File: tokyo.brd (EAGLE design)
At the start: 115 x 34 mm, 49 parts, among them J1 254-2X5F, J2 254-2X5M, P1 9774050151, P2 9774050151, P3 9774050151, P4 9774050151, Q1 STD6N95K5, T1 750313823, U1 UCC28710, X1 508-1X3B

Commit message: Changed values of R13 and R14 in order to get +5.5V on output.
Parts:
- R13: value 24k9 -> 22k6
- R14: value 121k -> 118k
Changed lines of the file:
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@@
 <attribute name="NAME" x="71.185" y="25.3856" size="1.016" layer="26" ratio="10" rot="SMR90"/>
 </element>
-<element name="R14" library="resistors" package="0603" value="121k" x="55.02" y="7.07" smashed="yes" rot="MR0">
+<element name="R14" library="resistors" package="0603" value="118k" x="55.02" y="7.07" smashed="yes" rot="MR0">
 <attribute name="NAME" x="56.5444" y="5.075" size="1.016" layer="26" ratio="10" rot="SMR0"/>
 </element>
-<element name="R13" library="resistors" package="0603" value="24k9" x="51.93" y="7.43" smashed="yes" rot="MR270">
+<element name="R13" library="resistors" package="0603" value="22k6" x="51.93" y="7.43" smashed="yes" rot="MR270">
 <attribute name="NAME" x="51.475" y="3.6456" size="1.016" layer="26" ratio="10" rot="SMR90"/>
 </element>

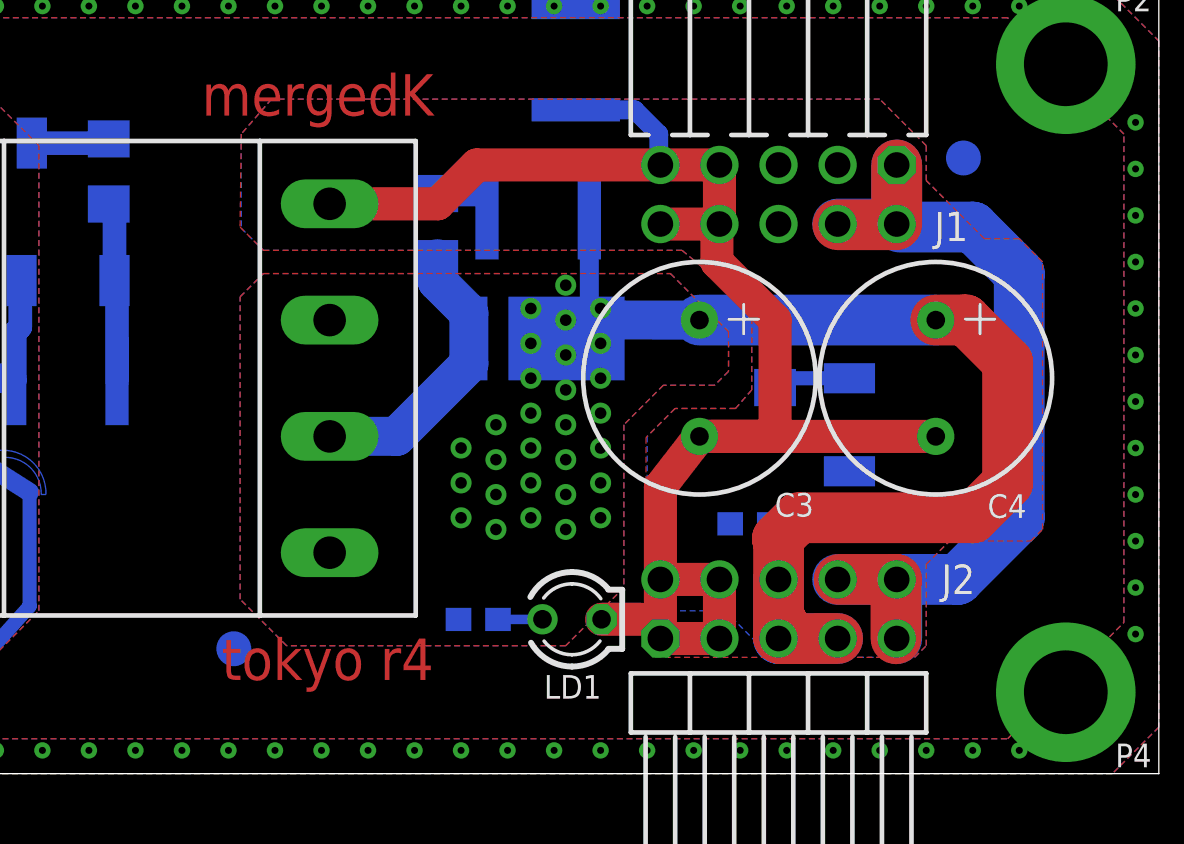
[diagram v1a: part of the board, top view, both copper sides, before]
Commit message: Corrected +5V/2 routing.
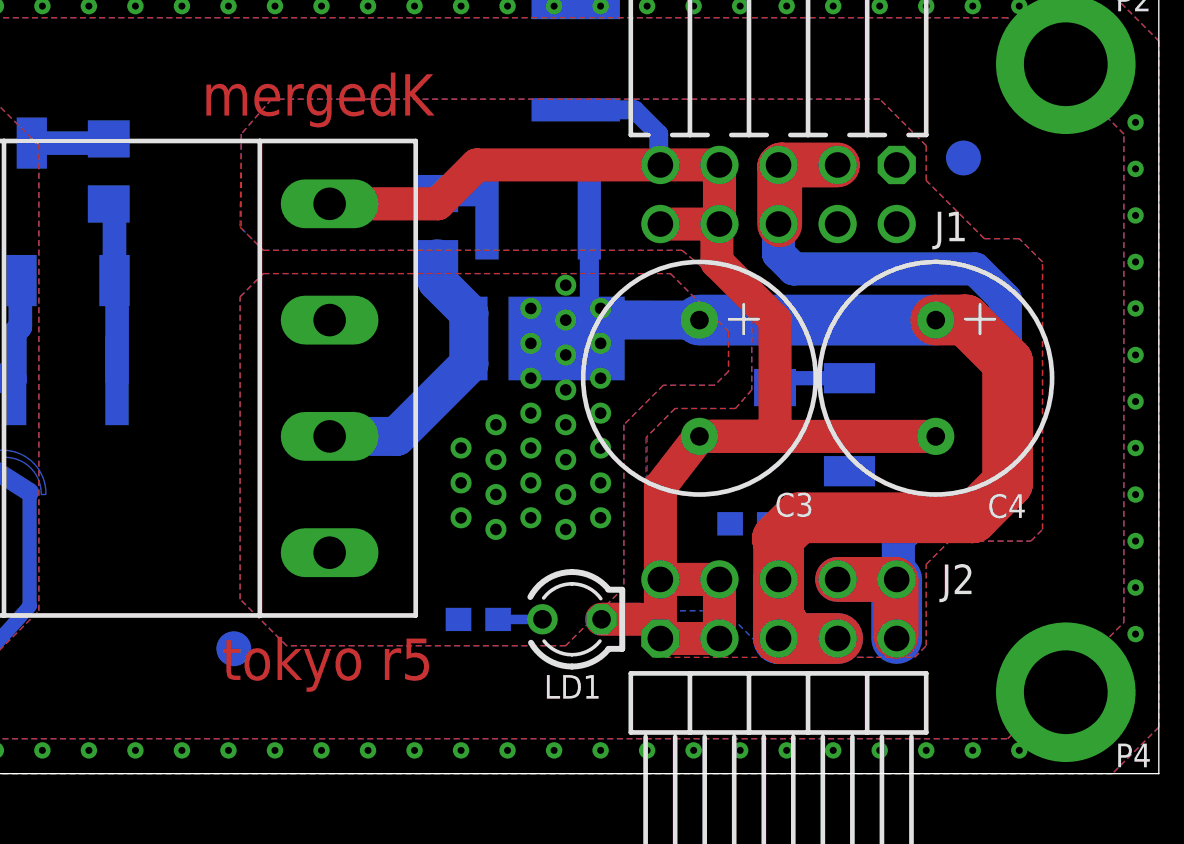
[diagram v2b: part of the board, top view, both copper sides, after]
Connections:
- net +5V/2: now also J1.3, J1.5, J1.6; no longer J1.1, J1.2, J1.4
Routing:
- net +5V/2: track 43.3 -> 47.2 mm
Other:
- board text added: "tokyo r5"
- board text removed: "tokyo r4"
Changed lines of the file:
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@@
 <?xml version="1.0" encoding="utf-8"?>
 <!DOCTYPE eagle SYSTEM "eagle.dtd">
-<eagle version="7.3.0">
+<eagle version="7.2.0">
 <drawing>
 <settings>
@@
 <setting verticaltext="up"/>
 </settings>
-<grid distance="1" unitdist="mm" unit="mm" style="lines" multiple="1" display="no" altdistance="0.1" altunitdist="mm" altunit="mm"/>
+<grid distance="39.3700787" unitdist="mil" unit="mil" style="lines" multiple="1" display="no" altdistance="3.93700787" altunitdist="mil" altunit="mil"/>
 <layers>
-<layer number="1" name="Top" color="4" fill="1" visible="no" active="yes"/>
+<layer number="1" name="Top" color="4" fill="1" visible="yes" active="yes"/>
 <layer number="2" name="Route2" color="1" fill="3" visible="no" active="no"/>
 <layer number="3" name="Route3" color="4" fill="3" visible="no" active="no"/>
 <layer number="14" name="Route14" color="1" fill="6" visible="no" active="no"/>
 <layer number="15" name="Route15" color="4" fill="6" visible="no" active="no"/>
-<layer number="16" name="Bottom" color="1" fill="1" visible="no" active="yes"/>
-<layer number="17" name="Pads" color="2" fill="1" visible="no" active="yes"/>
-<layer number="18" name="Vias" color="2" fill="1" visible="no" active="yes"/>
-<layer number="19" name="Unrouted" color="6" fill="1" visible="no" active="yes"/>
+<layer number="16" name="Bottom" color="1" fill="1" visible="yes" active="yes"/>
+<layer number="17" name="Pads" color="2" fill="1" visible="yes" active="yes"/>
+<layer number="18" name="Vias" color="2" fill="1" visible="yes" active="yes"/>
+<layer number="19" name="Unrouted" color="6" fill="1" visible="yes" active="yes"/>
 <layer number="20" name="Dimension" color="15" fill="1" visible="yes" active="yes"/>
 <layer number="21" name="tPlace" color="7" fill="1" visible="yes" active="yes"/>
 <layer number="22" name="bPlace" color="7" fill="1" visible="yes" active="yes"/>
-<layer number="23" name="tOrigins" color="15" fill="1" visible="no" active="yes"/>
-<layer number="24" name="bOrigins" color="15" fill="1" visible="no" active="yes"/>
+<layer number="23" name="tOrigins" color="15" fill="1" visible="yes" active="yes"/>
+<layer number="24" name="bOrigins" color="15" fill="1" visible="yes" active="yes"/>
 <layer number="25" name="tNames" color="7" fill="1" visible="yes" active="yes"/>
 <layer number="26" name="bNames" color="7" fill="1" visible="yes" active="yes"/>
 <layer number="27" name="tValues" color="7" fill="1" visible="no" active="yes"/>
 <layer number="28" name="bValues" color="7" fill="1" visible="no" active="yes"/>
-<layer number="29" name="tStop" color="7" fill="3" visible="no" active="yes"/>
-<layer number="30" name="bStop" color="7" fill="6" visible="no" active="yes"/>
+<layer number="29" name="tStop" color="7" fill="3" visible="yes" active="yes"/>
+<layer number="30" name="bStop" color="7" fill="6" visible="yes" active="yes"/>
 <layer number="31" name="tCream" color="7" fill="4" visible="no" active="yes"/>
 <layer number="32" name="bCream" color="7" fill="5" visible="no" active="yes"/>
@@
 <wire x1="0" y1="34" x2="0" y2="0" width="0" layer="20"/>
 <text x="83.819" y="28.292" size="1.778" layer="1" rot="SR0" align="bottom-right">mergedK</text>
-<text x="83.819" y="5.806" size="1.778" layer="1" rot="SR0" align="top-right">tokyo r4</text>
+<text x="83.819" y="5.806" size="1.778" layer="1" rot="SR0" align="top-right">tokyo r5</text>
 <text x="83.819" y="28.292" size="1.778" layer="29" align="bottom-right">mergedK</text>
-<text x="83.819" y="5.806" size="1.778" layer="29" align="top-right">tokyo r4</text>
+<text x="83.819" y="5.806" size="1.778" layer="29" align="top-right">tokyo r5</text>
 </plain>
 <attributes>
@@
 </signal>
 <signal name="+5V/2">
-<contactref element="J1" pad="1"/>
-<contactref element="J1" pad="4"/>
-<contactref element="J1" pad="2"/>
-<wire x1="103.73" y1="26.17" x2="103.73" y2="23.63" width="2.1844" layer="16"/>
 <contactref element="J2" pad="8"/>
 <contactref element="J2" pad="10"/>
 <contactref element="J2" pad="9"/>
-<wire x1="101.19" y1="8.35" x2="103.73" y2="8.35" width="2.1844" layer="16"/>
-<wire x1="103.73" y1="8.35" x2="106.35" y2="8.35" width="2.1844" layer="16"/>
-<wire x1="106.35" y1="8.35" x2="109" y2="11" width="2.1844" layer="16"/>
-<wire x1="109" y1="11" x2="109" y2="21.5" width="2.1844" layer="16"/>
-<wire x1="109" y1="21.5" x2="107" y2="23.5" width="2.1844" layer="16"/>
-<wire x1="107" y1="23.5" x2="103.86" y2="23.5" width="2.1844" layer="16"/>
-<wire x1="103.86" y1="23.5" x2="103.73" y2="23.63" width="1.6764" layer="16"/>
-<wire x1="103.73" y1="8.35" x2="103.65" y2="8.35" width="2.1844" layer="1"/>
 <wire x1="103.73" y1="5.81" x2="103.73" y2="8.35" width="2.1844" layer="16"/>
-<wire x1="101.25" y1="8.35" x2="103.65" y2="8.35" width="2.1844" layer="1"/>
-<wire x1="103.65" y1="8.35" x2="103.7" y2="8.3" width="2.1844" layer="1"/>
-<wire x1="103.7" y1="8.3" x2="103.7" y2="5.8" width="2.1844" layer="1"/>
-<wire x1="103.73" y1="23.63" x2="103.73" y2="26.17" width="2.1844" layer="1"/>
-<wire x1="101.19" y1="23.63" x2="103.73" y2="23.63" width="2.1844" layer="16"/>
-<wire x1="103.7" y1="23.6" x2="101.2" y2="23.6" width="2.1844" layer="1"/>
-<wire x1="101.19" y1="23.63" x2="101.2" y2="23.6" width="0" layer="19" extent="1-1"/>
+<contactref element="J1" pad="5"/>
+<contactref element="J1" pad="6"/>
+<contactref element="J1" pad="3"/>
+<wire x1="98.65" y1="23.63" x2="98.65" y2="26.17" width="1.6764" layer="16"/>
+<wire x1="101.19" y1="26.17" x2="98.65" y2="26.17" width="1.6764" layer="16"/>
+<wire x1="101.19" y1="8.35" x2="103.73" y2="8.35" width="1.9304" layer="16"/>
+<wire x1="101.19" y1="8.35" x2="103.65" y2="8.35" width="1.9304" layer="1"/>
+<wire x1="103.65" y1="8.35" x2="103.7" y2="8.3" width="1.9304" layer="1"/>
+<wire x1="103.7" y1="8.3" x2="103.7" y2="5.9" width="1.9304" layer="1"/>
+<wire x1="101.19" y1="26.17" x2="98.77" y2="26.17" width="1.9304" layer="1"/>
+<wire x1="98.77" y1="26.17" x2="98.7" y2="26.1" width="1.9304" layer="1"/>
+<wire x1="98.7" y1="26.1" x2="98.7" y2="23.6" width="1.9304" layer="1"/>
+<wire x1="98.65" y1="23.63" x2="98.65" y2="22.35" width="1.4224" layer="16"/>
+<wire x1="98.65" y1="22.35" x2="99.3" y2="21.7" width="1.4224" layer="16"/>
+<wire x1="99.3" y1="21.7" x2="107.1" y2="21.7" width="1.4224" layer="16"/>
+<wire x1="107.1" y1="21.7" x2="108.4" y2="20.4" width="1.4224" layer="16"/>
+<wire x1="108.4" y1="20.4" x2="108.4" y2="12.5" width="1.4224" layer="16"/>
+<wire x1="108.4" y1="12.5" x2="106.9" y2="11" width="1.4224" layer="16"/>
+<wire x1="106.9" y1="11" x2="104.7" y2="11" width="1.4224" layer="16"/>
+<wire x1="104.7" y1="11" x2="103.8" y2="10.1" width="1.4224" layer="16"/>
+<wire x1="103.8" y1="10.1" x2="103.8" y2="8.42" width="1.4224" layer="16"/>
+<wire x1="103.8" y1="8.42" x2="103.73" y2="8.35" width="1.4224" layer="16"/>
 </signal>
 <signal name="N$9">
